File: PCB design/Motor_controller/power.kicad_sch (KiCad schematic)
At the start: 47 parts, among them U10 TLP3555ATP1_F, U4 LD1117S33TR_SOT223, U5 LM3489MMX_NOPB, U6 LM3489MMX_NOPB, U7 TLP3555ATP1_F, U8 TLP3555ATP1_F, U9 TLP3555ATP1_F

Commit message: new file:   .gitignore 	new file:   .vscode/Motor_controller.mplab-local.json 	new file:   .vscode/Motor_controller.mplab.json 	new file:   .vscode/settings.json 	new file:   Firmware/Motor_controller.X/Motor_controller_default.bak0/components/FreeRTOS.yml 	new file:   Firmware/Motor_controller.X/Motor_controller_default.bak0/components/I2C/I2C.yml 	new file:   Firmware/Motor_controller.X/Motor_controller_default.bak0/components/I2C/components/sercom1.yml 	new file:   Firmware/Motor_controller.X/Motor_controller_default.bak0/components/O/O.yml 	new file:   Firmware/Motor_controller.X/Motor_controller_default.bak0/components/Sensor SPI/Sensor SPI.yml 	new file:   Firmware/Motor_controller.X/Motor_controller_default.bak0/components/Sensor SPI/components/sercom0.yml 	new file:   Firmware/Motor_controller.X/Motor_controller_default.bak0/components/Sensor SPU/Sensor SPU.yml 	new file:   Firmware/Motor_controller.X/Motor_controller_default.bak0/components/Ser/Ser.yml 	new file:   Firmware/Motor_controller.X/Motor_controller_default.bak0/components/Servo Motor/Servo Motor.yml 	new file:   Firmware/Motor_controller.X/Motor_controller_default.bak0/components/Servo Motor/components/sercom4.yml 	new file:   Firmware/Motor_controller.X/Motor_controller_default.bak0/components/UART/UART.yml 	new file:   Firmware/Motor_controller.X/Motor_controller_default.bak0/components/UART/components/sercom3.yml 	new file:   Firmware/Motor_controller.X/Motor_controller_default.bak0/components/UART/components/stdio.yml 	new file:   Firmware/Motor_controller.X/Motor_controller_default.bak0/components/cmsis.yml 	new file:   Firmware/Motor_controller.X/Motor_controller_default.bak0/components/core.yml 	new file:   Firmware/Motor_controller.X/Motor_controller_default.bak0/components/dfp.yml 	new file:   Firmware/Motor_controller.X/Motor_controller_default.bak0/components/eic.yml 	new file:   Firmware/Motor_controller.X/Motor_controller_default.bak0/components/evsys.yml 	new file:   Firmware/Motor_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
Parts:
- added R56, R57, R60, R62: 1M, Resistor_SMD:R_1206_3216Metric, symbol Device:R
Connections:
- net GND: now also R56.2, R57.2, R60.2, R62.2
- net VBLDC: now also R60.1
- net VPM: now also R62.1
- net VSM: now also R57.1
- net VServo: now also R56.1

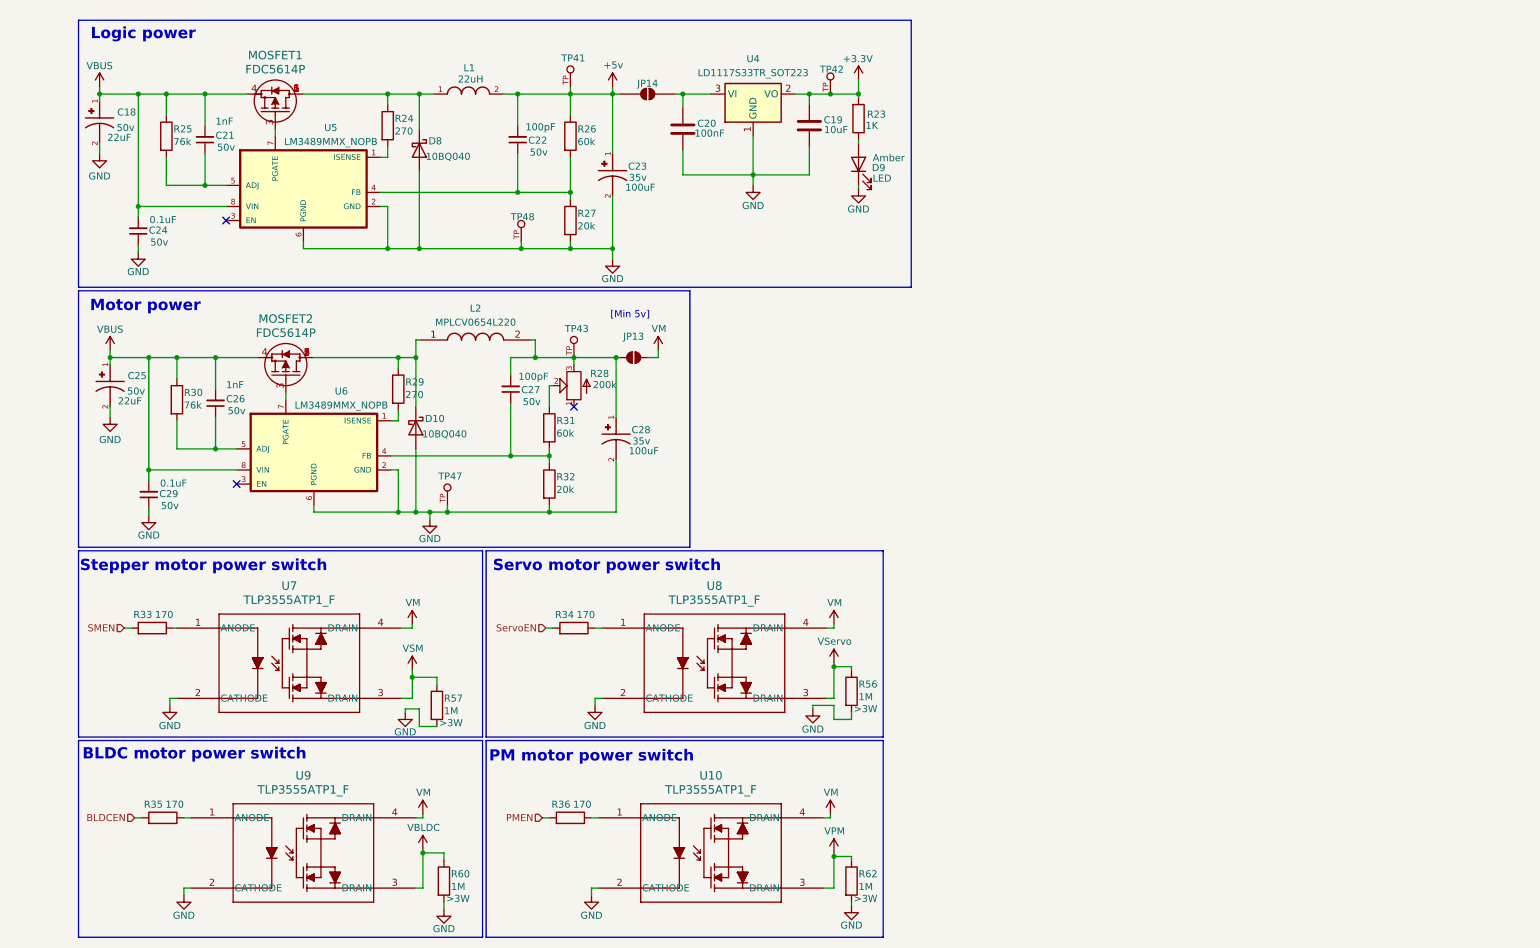
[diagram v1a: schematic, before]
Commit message: Implemented FOC controller
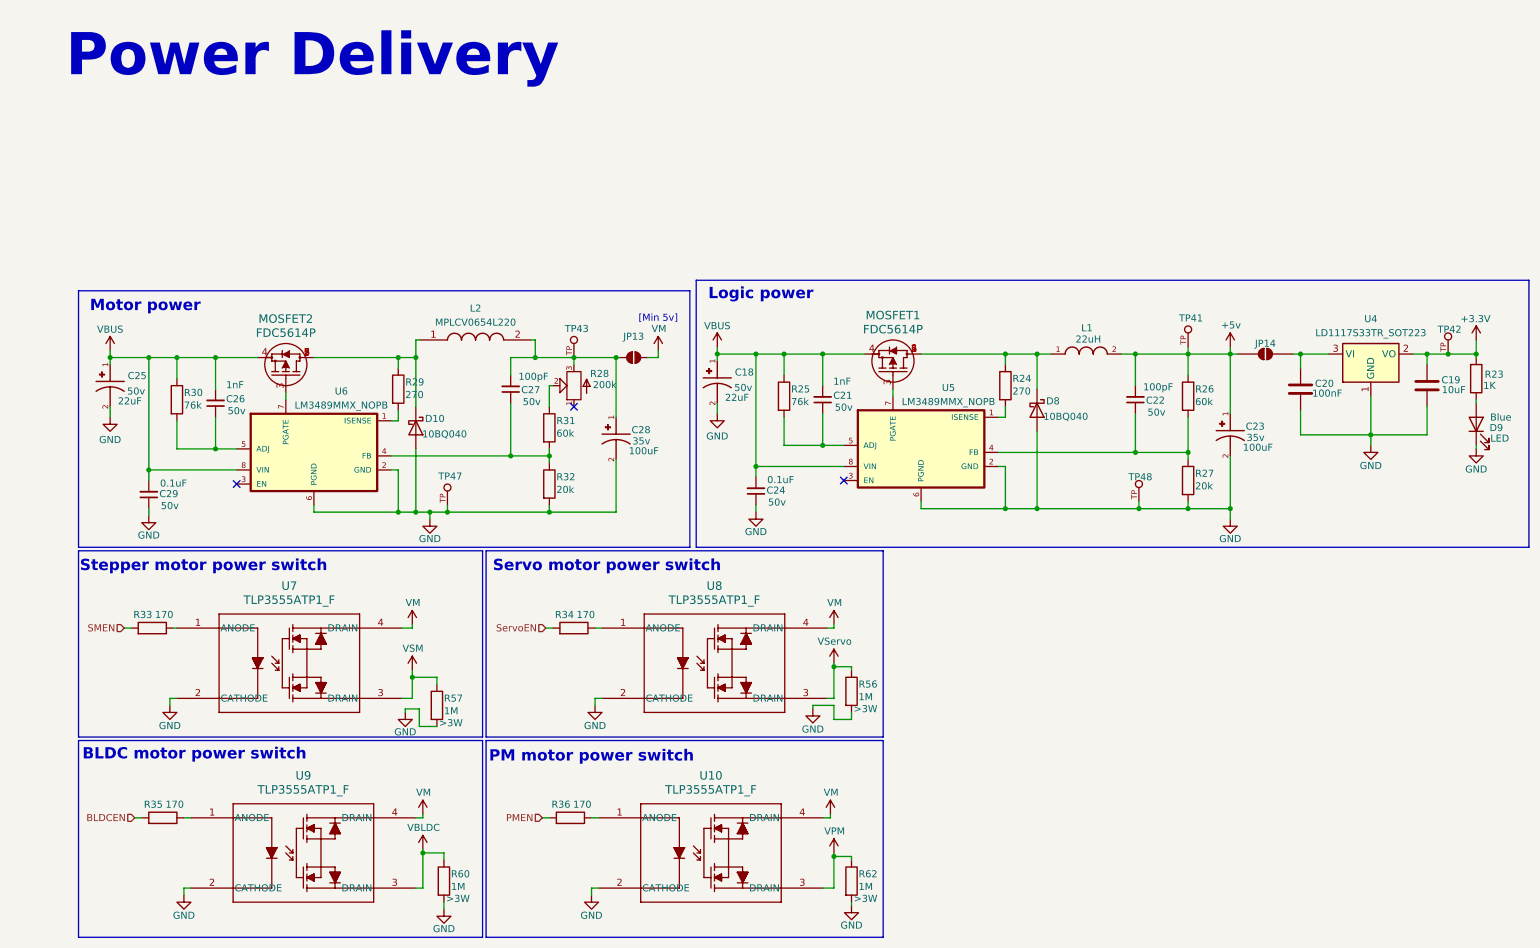
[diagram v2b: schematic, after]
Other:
- note added: "Power Delivery"
- moved on the sheet: C18, C19, C20, C21, C22, C23, C24, D8, D9, JP14, L1, MOSFET1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
